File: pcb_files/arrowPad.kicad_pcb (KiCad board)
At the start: 2 copper layers, 90.2 x 90.2 mm, 66 parts, among them J1 AudioJack3_Ground, J2 AudioJack3_Ground, K1 KEYSW, K10 KEYSW, K11 KEYSW, K12 KEYSW, K13 KEYSW, K14 KEYSW, K15 KEYSW, K16 KEYSW, K2 KEYSW, K3 KEYSW, K4 KEYSW, K5 KEYSW, K6 KEYSW, K7 KEYSW, K8 KEYSW, K9 KEYSW, U1 ProMicro, U2 NRF24L01_Breakout, U3 ADG417BN, U4 AMS1117-3.3, U5 ADG417BN, U6 ADG417BN, U7 TLC5940PWP

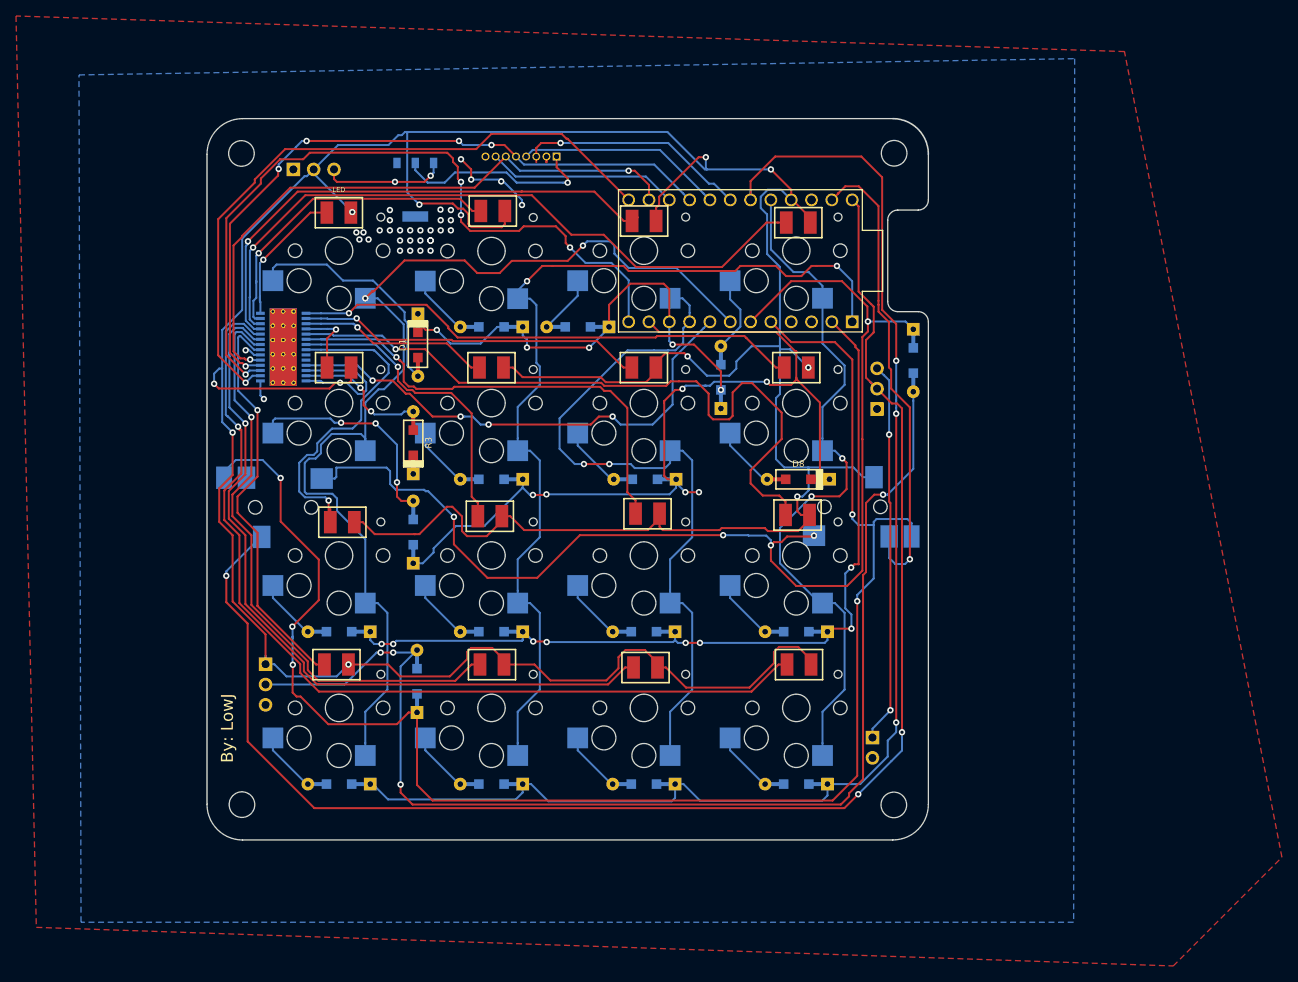
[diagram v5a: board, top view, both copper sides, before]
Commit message: re added mounting holes
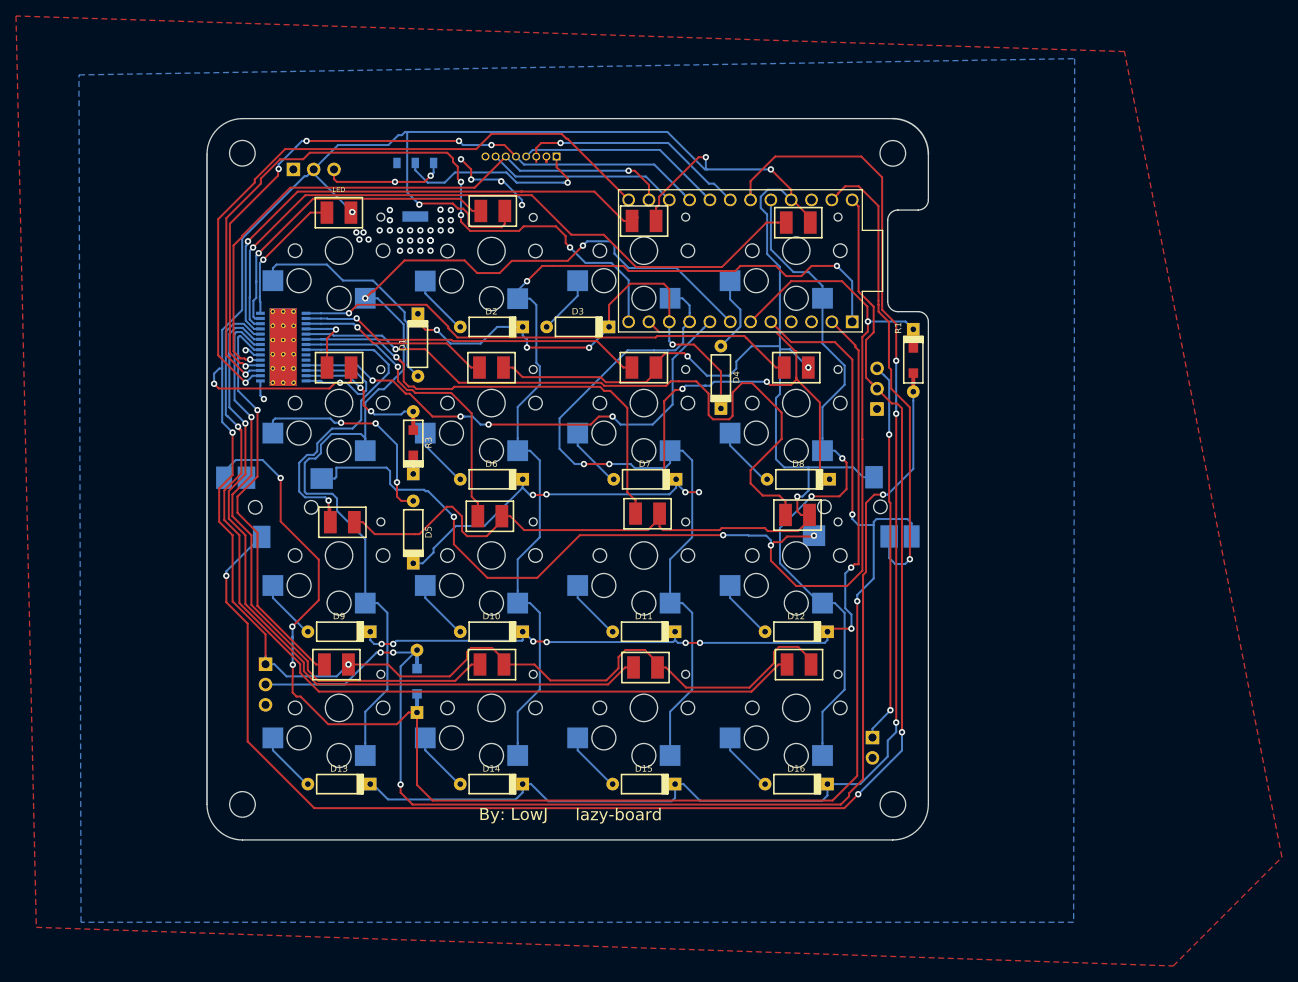
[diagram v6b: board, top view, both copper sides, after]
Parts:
- removed the REF** at (118.7, 134.0)
- removed the REF** at (118.6, 52.6)
- removed the REF** at (200.2, 52.6)
- removed the REF** at (200.2, 134.0)
- added REF**: MountingHole_3.2mm_M3, MountingHole:MountingHole_3.2mm_M3, F.Cu at (118.7, 134.0)
- added REF**: MountingHole_3.2mm_M3, MountingHole:MountingHole_3.2mm_M3, F.Cu at (118.7, 52.6)
- added REF**: MountingHole_3.2mm_M3, MountingHole:MountingHole_3.2mm_M3, F.Cu at (200.0, 52.6)
- added REF**: MountingHole_3.2mm_M3, MountingHole:MountingHole_3.2mm_M3, F.Cu at (200.0, 134.0)
- D1, D8: footprint keyboard_parts:D_SOD123_axial -> keyboard_parts:D_SOD123_axial_noSMD
- D10, D11, D12, D13, D14, D15, D16, D2, D3, D4, D5, D6, D7, D9: footprint keyboard_parts:D_SOD123_axial -> keyboard_parts:D_SOD123_axial_noSMD; moved to F.Cu
- R1: moved to F.Cu
- moved G*** 5.17 mm to (159.5, 102.9)
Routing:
- net /Row1: track 56.9 -> 61.1 mm, vias 5 -> 4
- net /Row2: track 111.3 -> 112.1 mm
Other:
- board text added: "lazy-board"
